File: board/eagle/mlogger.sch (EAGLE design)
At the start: 49 parts, among them J1 MICROSD-9P, SW1 SS-12D00G3, SW2 TVAF06-A020B-R, SW3 TVAF06-A020B-R

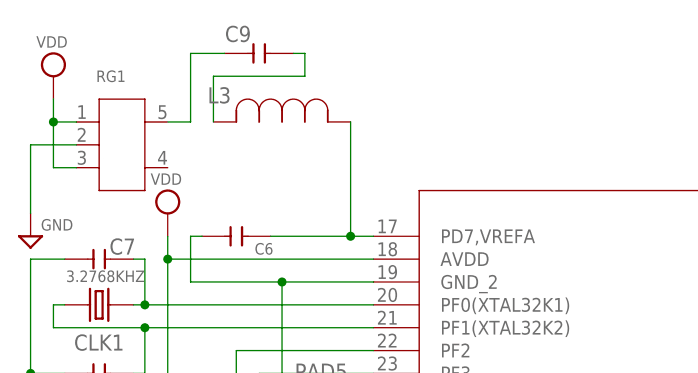
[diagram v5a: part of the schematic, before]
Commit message: レギュレータの接続ミス修正
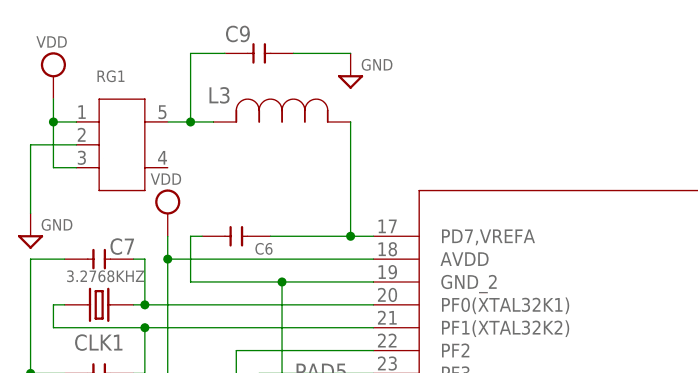
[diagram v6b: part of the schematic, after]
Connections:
- removed net N$9: C9.1, RG1.5
- net GND: now also C9.2
- net N$7: now also C9.1, RG1.5; no longer C9.2
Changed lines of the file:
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@@
 <part name="SUPPLY10" library="supply2" library_urn="urn:adsk.eagle:library:372" deviceset="VDD" device=""/>
 <part name="C9" library="MyParts" deviceset="MURATA_0603" device="" package3d_urn="urn:adsk.eagle:package:8004287/1"/>
+<part name="SUPPLY15" library="supply2" library_urn="urn:adsk.eagle:library:372" deviceset="GND" device=""/>
 </parts>
 <sheets>
@@
 <attribute name="NAME" x="-118.11" y="105.41" size="1.778" layer="95" ratio="10"/>
 <attribute name="VALUE" x="-118.11" y="101.6" size="1.27" layer="96" ratio="10"/>
+</instance>
+<instance part="SUPPLY15" gate="GND" x="-104.14" y="101.6" smashed="yes">
+<attribute name="VALUE" x="-102.997" y="102.235" size="1.27" layer="96"/>
 </instance>
 </instances>
@@
 <wire x1="-134.5946" y1="93.98" x2="-139.7" y2="93.98" width="0.1524" layer="91"/>
 </segment>
+<segment>
+<pinref part="C9" gate="G$1" pin="2"/>
+<pinref part="SUPPLY15" gate="GND" pin="GND"/>
+<wire x1="-110.49" y1="104.14" x2="-104.14" y2="104.14" width="0.1524" layer="91"/>
+</segment>
 </net>
 <net name="VDD" class="2">
@@
 <net name="N$7" class="0">
 <segment>
-<pinref part="L3" gate="A" pin="2"/>
-<pinref part="C9" gate="G$1" pin="2"/>
-<wire x1="-110.49" y1="104.14" x2="-109.22" y2="104.14" width="0.1524" layer="91"/>
-<wire x1="-109.22" y1="104.14" x2="-109.22" y2="101.6" width="0.1524" layer="91"/>
-<wire x1="-109.22" y1="101.6" x2="-119.38" y2="101.6" width="0.1524" layer="91"/>
-<wire x1="-119.38" y1="101.6" x2="-119.38" y2="96.52" width="0.1524" layer="91"/>
-</segment>
-</net>
-<net name="N$9" class="0">
-<segment>
 <pinref part="C9" gate="G$1" pin="1"/>
 <pinref part="RG1" gate="A" pin="5"/>
@@
 <wire x1="-121.92" y1="96.52" x2="-121.92" y2="104.14" width="0.1524" layer="91"/>
 <wire x1="-121.92" y1="104.14" x2="-118.11" y2="104.14" width="0.1524" layer="91"/>
-</segment>
-</net>
+<pinref part="L3" gate="A" pin="2"/>
+<wire x1="-121.92" y1="96.52" x2="-119.38" y2="96.52" width="0.1524" layer="91"/>
+<junction x="-121.92" y="96.52"/>
+</segment>
+</net>

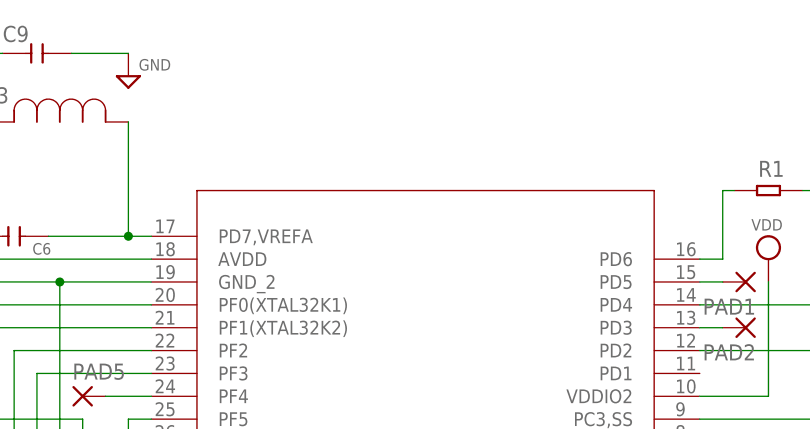
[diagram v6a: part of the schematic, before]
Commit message: GIOの間にGNDピンを追加。
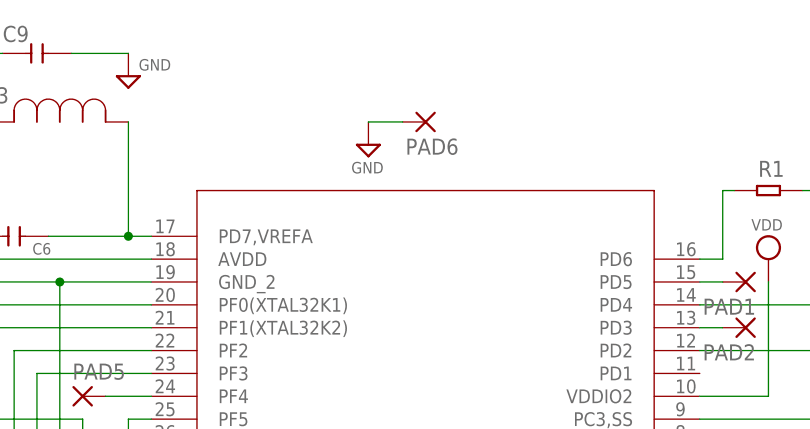
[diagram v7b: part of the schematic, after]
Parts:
- added PAD6: (no value), wirepad:1,6/0,8
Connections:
- net GND: now also PAD6.P
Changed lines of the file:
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@@
 <part name="C9" library="MyParts" deviceset="MURATA_0603" device="" package3d_urn="urn:adsk.eagle:package:8004287/1"/>
 <part name="SUPPLY15" library="supply2" library_urn="urn:adsk.eagle:library:372" deviceset="GND" device=""/>
+<part name="PAD6" library="wirepad" library_urn="urn:adsk.eagle:library:412" deviceset="1,6/0,8" device="" package3d_urn="urn:adsk.eagle:package:30830/1"/>
+<part name="SUPPLY26" library="supply2" library_urn="urn:adsk.eagle:library:372" deviceset="GND" device=""/>
 </parts>
 <sheets>
@@
 <instance part="SUPPLY15" gate="GND" x="-104.14" y="101.6" smashed="yes">
 <attribute name="VALUE" x="-102.997" y="102.235" size="1.27" layer="96"/>
+</instance>
+<instance part="PAD6" gate="P" x="-71.12" y="96.52" smashed="yes" rot="R180">
+<attribute name="NAME" x="-67.437" y="94.6658" size="1.778" layer="95" rot="R180"/>
+<attribute name="VALUE" x="-69.977" y="99.822" size="1.778" layer="96" rot="R180"/>
+</instance>
+<instance part="SUPPLY26" gate="GND" x="-77.47" y="93.98" smashed="yes">
+<attribute name="VALUE" x="-79.375" y="90.805" size="1.27" layer="96"/>
 </instance>
 </instances>
@@
 <wire x1="-110.49" y1="104.14" x2="-104.14" y2="104.14" width="0.1524" layer="91"/>
 </segment>
+<segment>
+<pinref part="SUPPLY26" gate="GND" pin="GND"/>
+<pinref part="PAD6" gate="P" pin="P"/>
+<wire x1="-77.47" y1="96.52" x2="-73.66" y2="96.52" width="0.1524" layer="91"/>
+</segment>
 </net>
